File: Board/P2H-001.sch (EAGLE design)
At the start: 26 parts, among them IC1 LTC485N, IC2 74LS07N, IC3 74LS157N, IC4 LTC485N, IC5 TLC5941NT, U1 ARDUINO_PRO_MINI

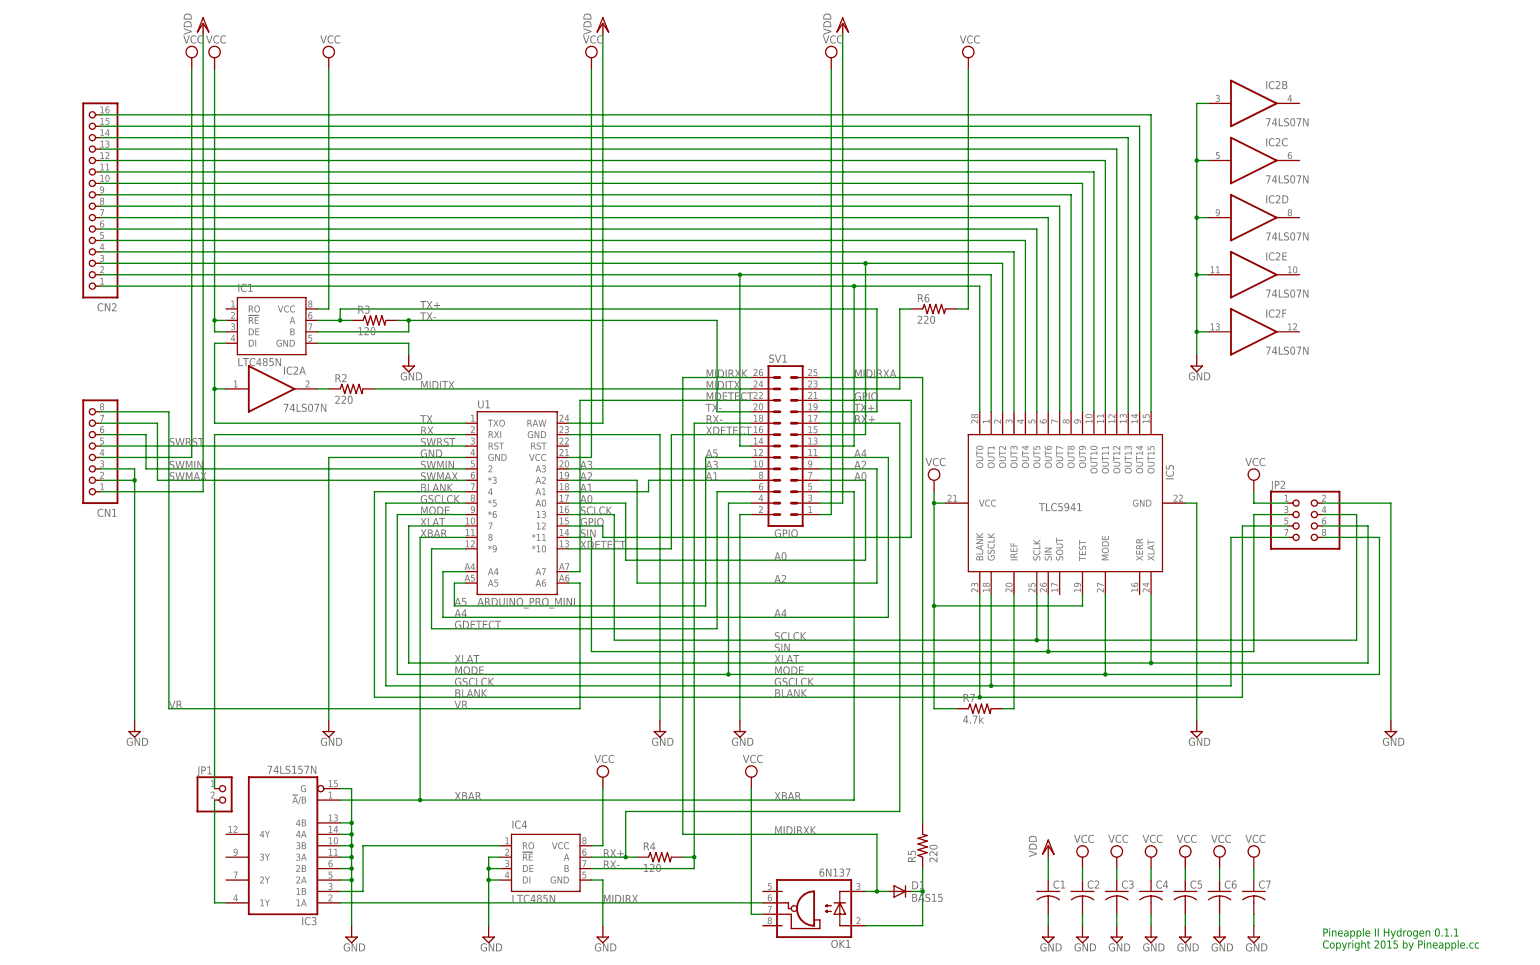
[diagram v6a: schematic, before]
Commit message: re-arranged board.
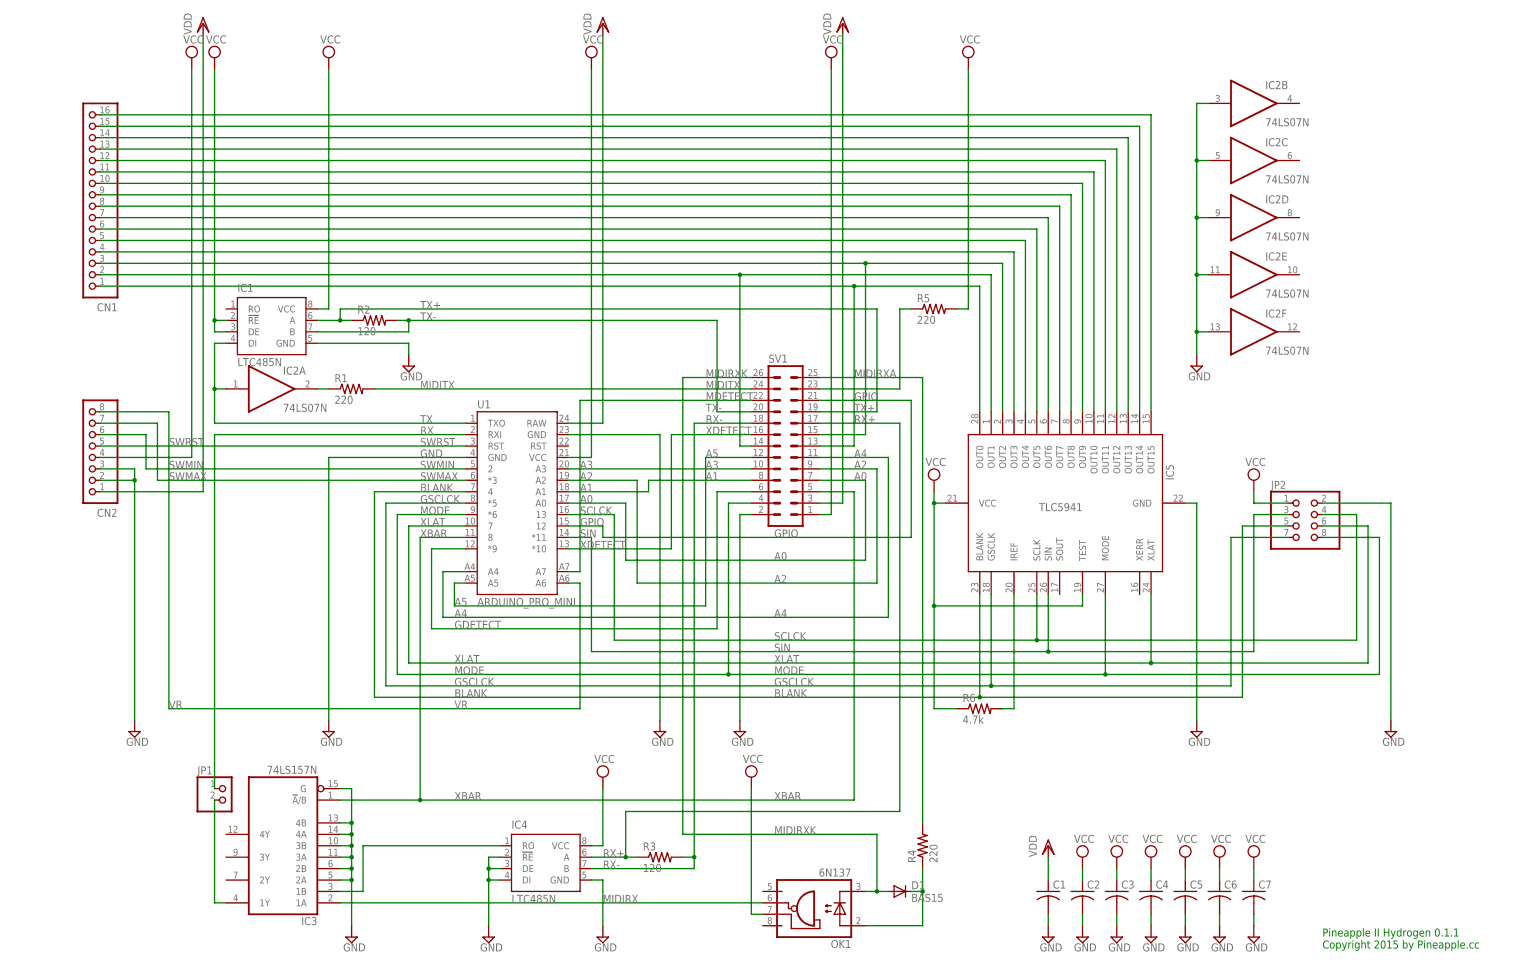
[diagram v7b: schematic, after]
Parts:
- removed R7: 4.7k, resistor:R-US_0204/5
- added R1: 220, resistor:R-US_0204/5
- CN1: device jst-ph:S8B-PH-K-S -> jst-ph:S16B-PH-K-S
- CN2: device jst-ph:S16B-PH-K-S -> jst-ph:S8B-PH-K-S
- R2: value 220 -> 120
- R4: value 120 -> 220
- R6: value 220 -> 4.7k
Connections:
- net GND: now also CN2.2, CN2.3; no longer CN1.2, CN1.3
- net LED2B: now also CN1.6; no longer CN2.6
- net LED2G: now also CN1.5; no longer CN2.5
- net LED3B: now also CN1.9; no longer CN2.9
- net LED3G: now also CN1.8; no longer CN2.8
- net LED3R: now also CN1.7; no longer CN2.7
- net LEDA: now also CN1.1; no longer CN2.1
- net MIDIRXA: now also R4.2; no longer R5.2
- net MIDITX: now also R1.2; no longer R2.2
- net N$12: now also CN1.2; no longer CN2.2
- net N$13: now also R4.1; no longer R5.1
- net N$14: now also CN1.3; no longer CN2.3
- net N$2: now also R1.1; no longer R2.1
- net N$24: now also CN1.15; no longer CN2.15
- net N$25: now also CN1.16; no longer CN2.16
- net N$3: now also CN1.13; no longer CN2.13
- net N$37: now also R6.2; no longer R7.2
- net N$4: now also R5.1; no longer R6.1
- net N$5: now also CN1.14; no longer CN2.14
- net N$6: now also CN1.10; no longer CN2.10
- net N$7: now also CN1.11; no longer CN2.11
- net N$8: now also CN1.12; no longer CN2.12
- net N$9: now also CN1.4; no longer CN2.4
- net RX+: now also R3.1; no longer R4.1
- net RX-: now also R3.2; no longer R4.2
- net SWMAX: now also CN2.7; no longer CN1.7
- net SWMIN: now also CN2.6; no longer CN1.6
- net SWRST: now also CN2.5; no longer CN1.5
- net TX+: now also R2.1; no longer R3.1
- net TX-: now also R2.2; no longer R3.2
- net VCC: now also CN2.4, R5.2, R6.1; no longer CN1.4, R6.2, R7.1
- net VDD: now also CN2.1; no longer CN1.1
- net VR: now also CN2.8; no longer CN1.8
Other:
- moved on the sheet: R2, R3, R4, R5, R6

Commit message: New design.
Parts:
- removed JP2: (no value), pinhead:PINHD-2X4
- added SV2: (no value), con-ml:ML10
- C1: value (none) -> 0.1u
- C2, C3, C4, C5, C6, C7: value (none) -> 0.01u
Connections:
- net BLANK: now also SV2.5; no longer JP2.5
- net GND: now also SV2.10, SV2.2; no longer JP2.2
- net GSCLCK: now also SV2.7; no longer JP2.7
- net MODE: now also SV2.8; no longer JP2.8
- net SCLCK: now also SV2.4; no longer JP2.4
- net SIN: now also SV2.3; no longer JP2.3
- net VCC: now also SV2.1; no longer JP2.1
- net VDD: now also SV2.9
- net XLAT: now also SV2.6; no longer JP2.6
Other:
- note added: "Pineapple II Hydrogen 0.2.0 Copyright 2015 by Pineapple.cc"
- note removed: "Pineapple II Hydrogen 0.1.1 Copyright 2015 by Pineapple.cc"
- moved on the sheet: C1, C2, C3, C4, C5, C6, C7
